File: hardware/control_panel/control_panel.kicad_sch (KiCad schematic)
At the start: 9 parts

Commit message: KiCad changes
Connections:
- net +5V: no longer SW_Inspection_Light1.5 (B)
- net 3V3+: now also SW_Inspection_Light1.5 (B)
- net BUZZER: now also ESP32-S3SM1.1 (GP1); no longer ESP32-S3SM1.13 (GP13)
- net IN1_FAN: now also ESP32-S3SM1.12 (GP12); no longer ESP32-S3SM1.11 (GP11)
- net IN2_LEDS: now also ESP32-S3SM1.13 (GP13); no longer ESP32-S3SM1.12 (GP12)
- net INSP_LITE_5+ renamed INSP_LITE_3.3V+
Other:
- moved on the sheet: 5VGND1, Buzzer_Conn_01x02_1, SW_Inspection_Light1
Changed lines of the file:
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@@
-	)
-	(junction
-		(at 148.59 80.01)
-		(diameter 0)
-		(color 0 0 0 0)
 	)
 	(junction
@@
 	(wire
 		(pts
-			(xy 148.59 80.01) (xy 171.45 80.01)
+			(xy 146.05 105.41) (xy 146.05 80.01)
+		)
+		(stroke
+			(width 0)
+			(type default)
+		)
+	)
+	(wire
+		(pts
+			(xy 91.44 120.65) (xy 102.87 120.65)
 		)
 		(stroke
@@
 	(wire
 		(pts
+			(xy 128.27 124.46) (xy 160.02 124.46)
+		)
+		(stroke
+			(width 0)
+			(type default)
+		)
+	)
+	(wire
+		(pts
 			(xy 102.87 128.27) (xy 101.6 128.27)
 		)
@@
 	(wire
 		(pts
-			(xy 148.59 77.47) (xy 148.59 80.01)
-		)
-		(stroke
-			(width 0)
-			(type default)
-		)
-	)
-	(wire
-		(pts
-			(xy 162.56 110.49) (xy 162.56 132.08)
-		)
-		(stroke
-			(width 0)
-			(type default)
-		)
-	)
-	(wire
-		(pts
-			(xy 128.27 132.08) (xy 162.56 132.08)
+			(xy 162.56 110.49) (xy 162.56 128.27)
 		)
 		(stroke
@@
 	(wire
 		(pts
-			(xy 148.59 80.01) (xy 148.59 96.52)
-		)
-		(stroke
-			(width 0)
-			(type default)
-		)
-	)
-	(wire
-		(pts
-			(xy 160.02 107.95) (xy 160.02 128.27)
-		)
-		(stroke
-			(width 0)
-			(type default)
-		)
-	)
-	(wire
-		(pts
-			(xy 160.02 128.27) (xy 128.27 128.27)
+			(xy 137.16 77.47) (xy 137.16 113.03)
+		)
+		(stroke
+			(width 0)
+			(type default)
+		)
+	)
+	(wire
+		(pts
+			(xy 160.02 107.95) (xy 160.02 124.46)
 		)
 		(stroke
@@
 	(wire
 		(pts
-			(xy 170.18 92.71) (xy 157.48 92.71)
+			(xy 78.74 86.36) (xy 91.44 86.36)
 		)
 		(stroke
@@
 	(wire
 		(pts
-			(xy 148.59 96.52) (xy 137.16 96.52)
+			(xy 128.27 128.27) (xy 162.56 128.27)
 		)
 		(stroke
@@
 	(wire
 		(pts
-			(xy 128.27 124.46) (xy 157.48 124.46)
-		)
-		(stroke
-			(width 0)
-			(type default)
-		)
-	)
-	(wire
-		(pts
 			(xy 146.05 105.41) (xy 146.05 120.65)
 		)
@@
 	(wire
 		(pts
-			(xy 185.42 67.31) (xy 209.55 67.31)
+			(xy 185.42 77.47) (xy 209.55 77.47)
 		)
 		(stroke
@@
 	(wire
 		(pts
-			(xy 146.05 77.47) (xy 146.05 78.74)
+			(xy 134.62 77.47) (xy 134.62 78.74)
 		)
 		(stroke
@@
 	(wire
 		(pts
-			(xy 171.45 69.85) (xy 171.45 80.01)
-		)
-		(stroke
-			(width 0)
-			(type default)
-		)
-	)
-	(wire
-		(pts
 			(xy 63.5 143.51) (xy 102.87 143.51)
 		)
@@
 	(wire
 		(pts
-			(xy 209.55 67.31) (xy 209.55 64.77)
+			(xy 209.55 77.47) (xy 209.55 64.77)
 		)
 		(stroke
@@
 	(wire
 		(pts
-			(xy 157.48 92.71) (xy 157.48 124.46)
+			(xy 91.44 86.36) (xy 91.44 120.65)
 		)
 		(stroke
@@
 	(wire
 		(pts
-			(xy 137.16 96.52) (xy 137.16 113.03)
+			(xy 146.05 80.01) (xy 175.26 80.01)
 		)
 		(stroke
@@
 	(wire
 		(pts
-			(xy 175.26 92.71) (xy 189.23 92.71)
-		)
-		(stroke
-			(width 0)
-			(type default)
-		)
-	)
-	(wire
-		(pts
-			(xy 171.45 69.85) (xy 175.26 69.85)
+			(xy 73.66 86.36) (xy 59.69 86.36)
 		)
 		(stroke
@@
 	)
 	(label "BUZZER"
-		(at 130.81 124.46 0)
-		(effects
-			(font
-				(size 1.27 1.27)
-			)
-			(justify left bottom)
-		)
-	)
-	(label "+5V"
-		(at 156.21 80.01 180)
-		(effects
-			(font
-				(size 1.27 1.27)
-			)
-			(justify right bottom)
+		(at 93.98 120.65 0)
+		(effects
+			(font
+				(size 1.27 1.27)
+			)
+			(justify left bottom)
 		)
 	)
@@
 		)
 	)
-	(label "INSP_LITE_5+"
-		(at 189.23 67.31 0)
+	(label "INSP_LITE_3.3V+"
+		(at 189.23 77.47 0)
 		(effects
 			(font
@@
 	(symbol
 		(lib_id "Switch:SW_Push_DPDT")
-		(at 180.34 64.77 0)
+		(at 180.34 74.93 0)
 		(unit 1)
 		(exclude_from_sim no)
@@
 		(fields_autoplaced yes)
 		(property "Reference" "SW_Inspection_Light1"
-			(at 180.34 50.8 0)
+			(at 180.34 60.96 0)
 			(effects
 				(font
@@
 		)
 		(property "Value" "SW_Push_DPDT"
-			(at 180.34 53.34 0)
+			(at 180.34 63.5 0)
 			(effects
 				(font
@@
 		)
 		(property "Footprint" "TMB_Library:SW_Push_DPDT_8x8mm"
-			(at 180.34 59.69 0)
+			(at 180.34 69.85 0)
 			(effects
 				(font
@@
 		)
 		(property "Datasheet" "~"
-			(at 180.34 59.69 0)
+			(at 180.34 69.85 0)
 			(effects
 				(font
@@
 		)
 		(property "Description" "Momentary Switch, dual pole double throw"
-			(at 180.34 64.77 0)
+			(at 180.34 74.93 0)
 			(effects
 				(font
@@
 	(symbol
 		(lib_id "power:GND")
-		(at 146.05 78.74 0)
+		(at 134.62 78.74 0)
 		(unit 1)
 		(exclude_from_sim no)
@@
 		(fields_autoplaced yes)
 		(property "Reference" "#PWR06"
-			(at 146.05 85.09 0)
+			(at 134.62 85.09 0)
 			(effects
 				(font
@@
 		)
 		(property "Value" "GND"
-			(at 146.05 83.82 0)
+			(at 134.62 83.82 0)
 			(effects
 				(font
@@
 		)
 		(property "Footprint" ""
-			(at 146.05 78.74 0)
+			(at 134.62 78.74 0)
 			(effects
 				(font
@@
 		)
 		(property "Datasheet" ""
-			(at 146.05 78.74 0)
+			(at 134.62 78.74 0)
 			(effects
 				(font
@@
 		)
 		(property "Description" "Power symbol creates a global label with name \"GND\" , ground"
-			(at 146.05 78.74 0)
+			(at 134.62 78.74 0)
 			(effects
 				(font
@@
 	(symbol
 		(lib_id "Connector:Conn_01x02_Pin")
-		(at 148.59 72.39 270)
+		(at 137.16 72.39 270)
 		(unit 1)
 		(exclude_from_sim no)
@@
 		(fields_autoplaced yes)
 		(property "Reference" "5VGND1"
-			(at 149.86 71.7549 90)
+			(at 138.43 71.7549 90)
 			(effects
 				(font
@@
 		)
 		(property "Value" "Conn_01x02_Pin"
-			(at 149.86 74.2949 90)
+			(at 138.43 74.2949 90)
 			(effects
 				(font
@@
 		)
 		(property "Footprint" "Connector_JST:JST_XH_B2B-XH-A_1x02_P2.50mm_Vertical"
-			(at 148.59 72.39 0)
+			(at 137.16 72.39 0)
 			(effects
 				(font
@@
 		)
 		(property "Datasheet" "~"
-			(at 148.59 72.39 0)
+			(at 137.16 72.39 0)
 			(effects
 				(font
@@
 		)
 		(property "Description" "Generic connector, single row, 01x02, script generated"
-			(at 148.59 72.39 0)
+			(at 137.16 72.39 0)
 			(effects
 				(font
@@
 	(symbol
 		(lib_id "Device:Buzzer")
-		(at 172.72 90.17 90)
+		(at 76.2 83.82 270)
+		(mirror x)
 		(unit 1)
 		(exclude_from_sim no)
@@
 		(fields_autoplaced yes)
 		(property "Reference" "Buzzer_Conn_01x02_1"
-			(at 176.53 88.1448 90)
+			(at 72.39 81.7948 90)
 			(effects
 				(font
@@
 		)
 		(property "Value" "Buzzer"
-			(at 176.53 90.6848 90)
+			(at 72.39 84.3348 90)
 			(effects
 				(font
@@
 		)
 		(property "Footprint" "Connector_PinHeader_2.54mm:PinHeader_1x02_P2.54mm_Vertical"
-			(at 170.18 90.805 90)
+			(at 78.74 84.455 90)
 			(effects
 				(font
@@
 		)
 		(property "Datasheet" "~"
-			(at 170.18 90.805 90)
+			(at 78.74 84.455 90)
 			(effects
 				(font
@@
 		)
 		(property "Description" "Buzzer, polarized"
-			(at 172.72 90.17 0)
+			(at 76.2 83.82 0)
 			(effects
 				(font
@@
 	(symbol
 		(lib_id "power:GND")
-		(at 189.23 92.71 90)
+		(at 59.69 86.36 270)
+		(mirror x)
 		(unit 1)
 		(exclude_from_sim no)
@@
 		(fields_autoplaced yes)
 		(property "Reference" "#PWR09"
-			(at 195.58 92.71 0)
+			(at 53.34 86.36 0)
 			(effects
 				(font
@@
 		)
 		(property "Value" "GND"
-			(at 193.04 92.7099 90)
+			(at 55.88 86.3599 90)
 			(effects
 				(font
@@
 		)
 		(property "Footprint" ""
-			(at 189.23 92.71 0)
+			(at 59.69 86.36 0)
 			(effects
 				(font
@@
 		)
 		(property "Datasheet" ""
-			(at 189.23 92.71 0)
+			(at 59.69 86.36 0)
 			(effects
 				(font
@@
 		)
 		(property "Description" "Power symbol creates a global label with name \"GND\" , ground"
-			(at 189.23 92.71 0)
-			(effects
-				(font
+			(at 59.69 86.36 0)
+			(effects
+				(font

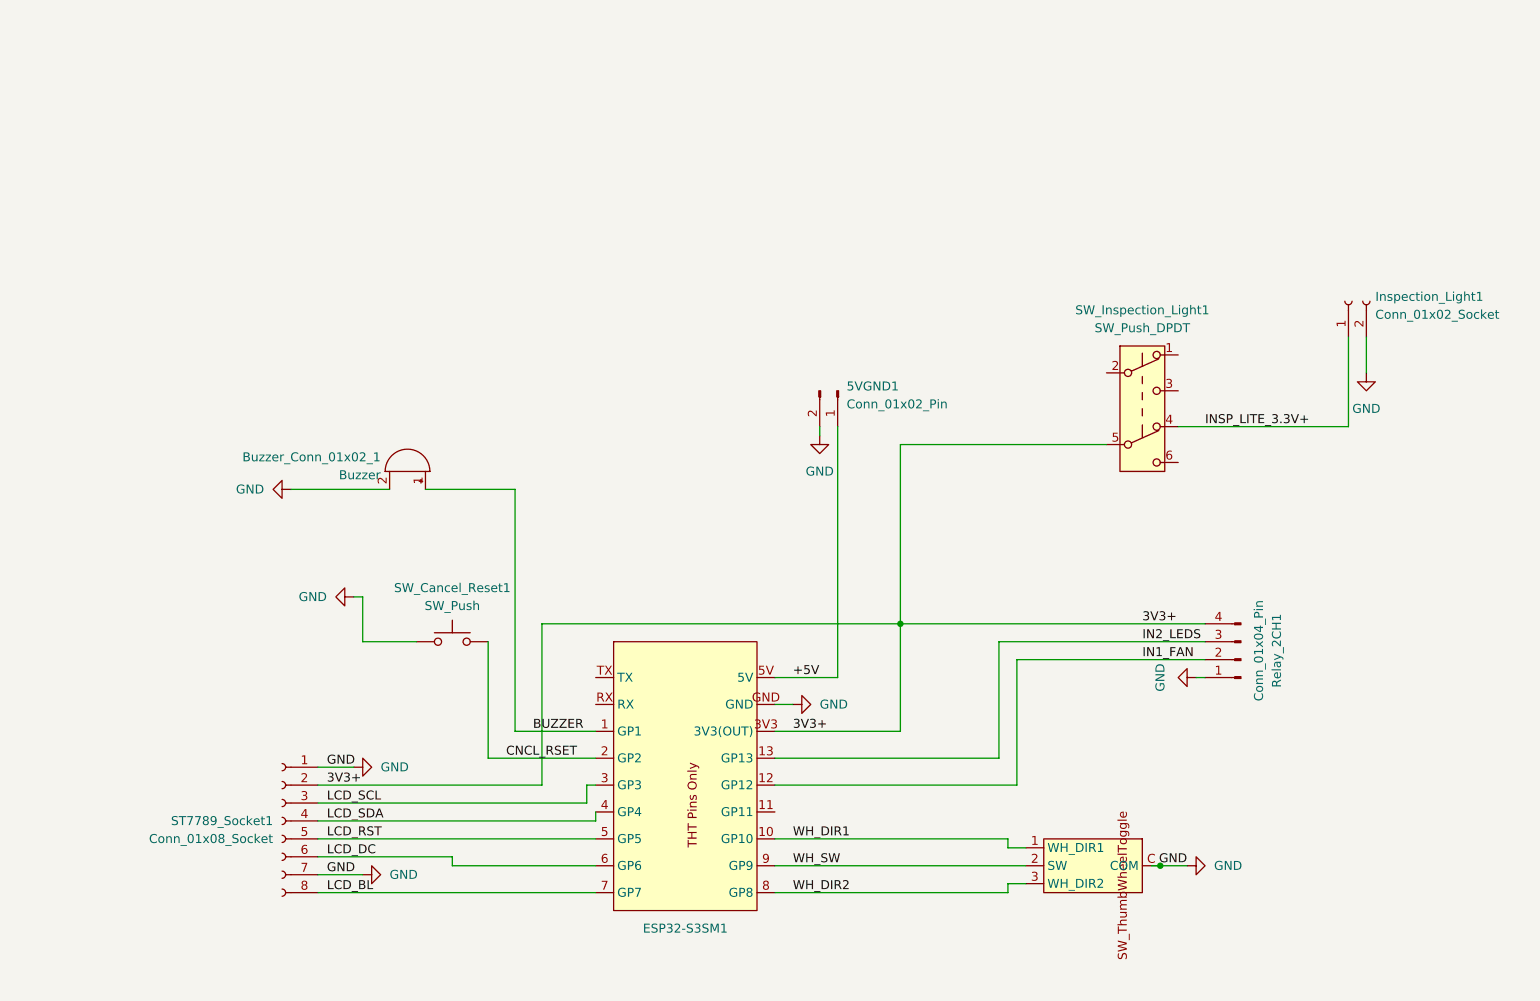
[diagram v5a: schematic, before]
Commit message: KiCad - ESP32-S3 Super Mini B.Cu - Fix for flipped connections
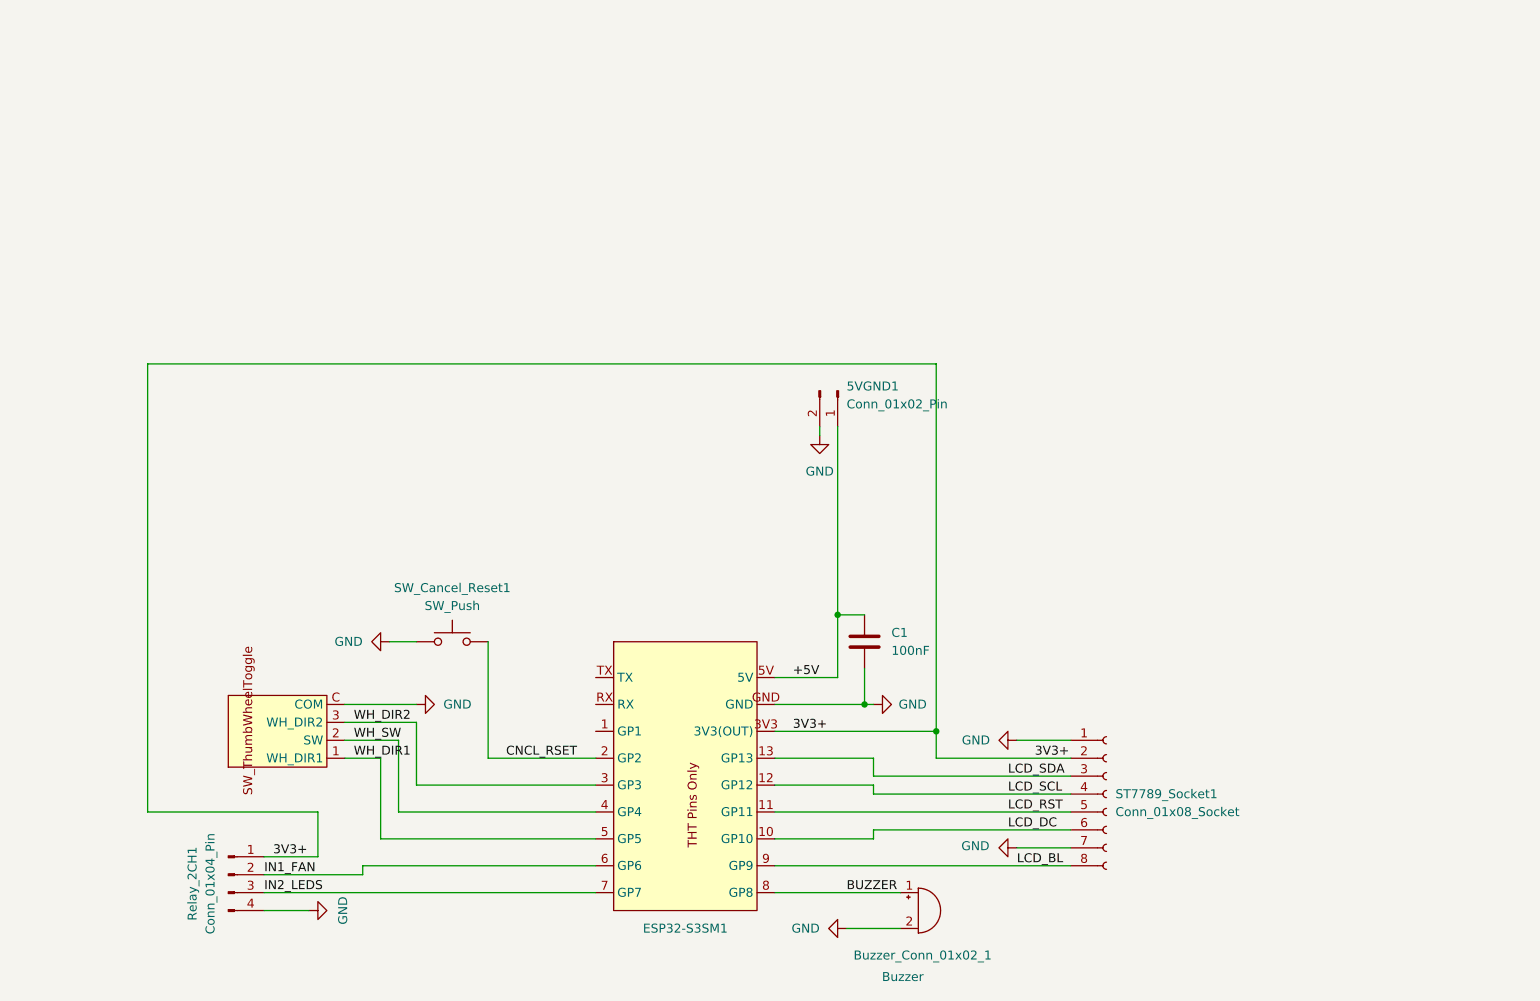
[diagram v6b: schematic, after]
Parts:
- removed Inspection_Light1: Conn_01x02_Socket, Connector_PinHeader_2.54mm:PinHeader_1x02_P2.54mm_Vertical, symbol Connector:Conn_01x02_Socket
- removed SW_Inspection_Light1: SW_Push_DPDT, TMB_Library:SW_Push_DPDT_8x8mm, symbol Switch:SW_Push_DPDT
- added C1: 100nF, Capacitor_THT:C_Disc_D6.0mm_W2.5mm_P5.00mm, symbol Device:C
- Buzzer_Conn_01x02_1: footprint Connector_PinHeader_2.54mm:PinHeader_1x02_P2.54mm_Vertical -> Connector_JST:JST_XH_B2B-XH-A_1x02_P2.50mm_Vertical
- ESP32-S3SM1: footprint TMB_Library:ESP32-S3_Super_Mini_THTONLY -> TMB_Library:ESP32-S3_Super_Mini_THTONLY_(B.Cu)
- Relay_2CH1: footprint Connector_PinHeader_2.54mm:PinHeader_1x04_P2.54mm_Vertical -> Connector_JST:JST_XH_B4B-XH-A_1x04_P2.50mm_Vertical
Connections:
- net +5V: now also C1.1
- net 3V3+: now also Relay_2CH1.1 (Pin_1); no longer Relay_2CH1.4 (Pin_4)
- net BUZZER: now also ESP32-S3SM1.8 (GP8); no longer ESP32-S3SM1.1 (GP1)
- net GND: now also Relay_2CH1.4 (Pin_4), C1.2; no longer Relay_2CH1.1 (Pin_1)
- net IN1_FAN: now also ESP32-S3SM1.6 (GP6); no longer ESP32-S3SM1.12 (GP12)
- net IN2_LEDS: now also ESP32-S3SM1.7 (GP7); no longer ESP32-S3SM1.13 (GP13)
- net LCD_BL: now also ESP32-S3SM1.9 (GP9); no longer ESP32-S3SM1.7 (GP7)
- net LCD_DC: now also ESP32-S3SM1.10 (GP10); no longer ESP32-S3SM1.6 (GP6)
- net LCD_RST: now also ESP32-S3SM1.11 (GP11); no longer ESP32-S3SM1.5 (GP5)
- net LCD_SCL: now also ESP32-S3SM1.12 (GP12), ST7789_Socket1.4 (Pin_4); no longer ESP32-S3SM1.3 (GP3), ST7789_Socket1.3 (Pin_3)
- net LCD_SDA: now also ESP32-S3SM1.13 (GP13), ST7789_Socket1.3 (Pin_3); no longer ESP32-S3SM1.4 (GP4), ST7789_Socket1.4 (Pin_4)
- net WH_DIR1: now also ESP32-S3SM1.5 (GP5); no longer ESP32-S3SM1.10 (GP10)
- net WH_DIR2: now also ESP32-S3SM1.3 (GP3); no longer ESP32-S3SM1.8 (GP8)
- net WH_SW: now also ESP32-S3SM1.4 (GP4); no longer ESP32-S3SM1.9 (GP9)
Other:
- moved on the sheet: Buzzer_Conn_01x02_1, Relay_2CH1, ST7789_Socket1

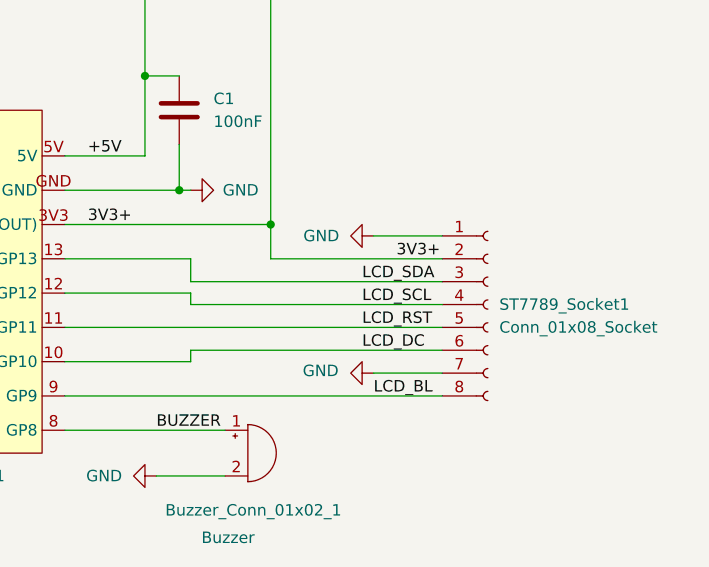
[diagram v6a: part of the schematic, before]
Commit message: Fix: LCD SCL SDA mixup
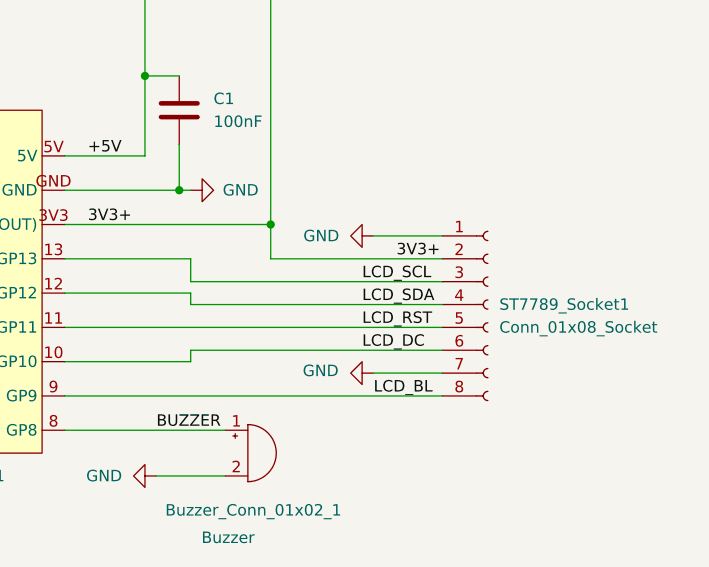
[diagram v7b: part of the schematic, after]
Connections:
- net LCD_SCL: now also ESP32-S3SM1.13 (GP13), ST7789_Socket1.3 (Pin_3); no longer ESP32-S3SM1.12 (GP12), ST7789_Socket1.4 (Pin_4)
- net LCD_SDA: now also ESP32-S3SM1.12 (GP12), ST7789_Socket1.4 (Pin_4); no longer ESP32-S3SM1.13 (GP13), ST7789_Socket1.3 (Pin_3)
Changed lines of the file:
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@@
-		)
-	)
-	(label "LCD_SCL"
-		(at 161.29 129.54 0)
-		(effects
-			(font
-				(size 1.27 1.27)
-			)
-			(justify left bottom)
 		)
 	)
@@
 		)
 	)
-	(label "LCD_SDA"
+	(label "LCD_SCL"
 		(at 161.29 127 0)
 		(effects
 			(font
+				(size 1.27 1.27)
+			)
+			(justify left bottom)
+		)
+	)
+	(label "LCD_SDA"
+		(at 161.29 129.54 0)
+		(effects
+			(font
